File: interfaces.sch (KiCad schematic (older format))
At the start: 55 parts, among them J6 0878311420, J7 61300611121, U14 XC7A100T-FGG484, U17 EMMC04G-S100-B08U, U18 MAX3421EEHJ, U19 FT245RQ, U6 NVT2008DQ,115, Y1 ABM8G-12.000MHZ-18-D2Y-T

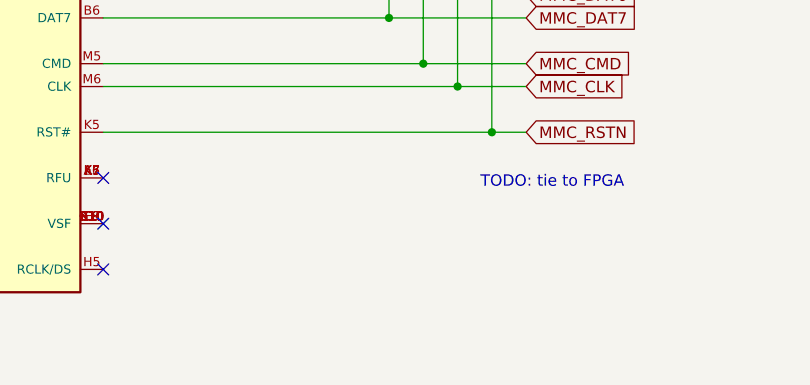
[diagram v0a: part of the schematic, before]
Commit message: Specify eMMC model
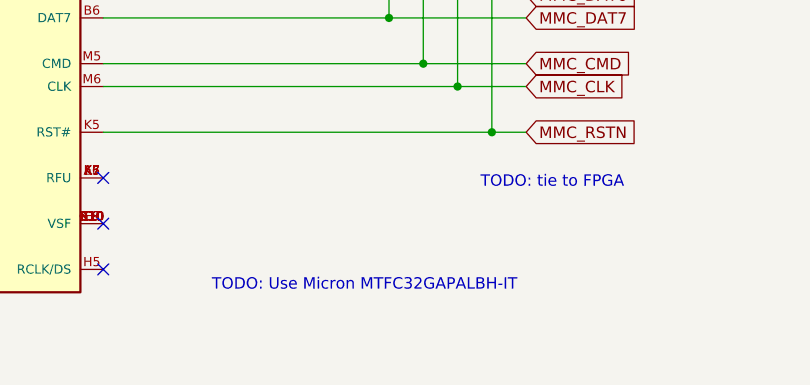
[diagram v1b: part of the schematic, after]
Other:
- note added: "TODO: Use Micron MTFC32GAPALBH-IT"
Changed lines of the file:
@@
 Text GLabel 8725 6150 0    50   Input ~ 0
 SPI0_CLK
+Text Notes 5125 10800 0    50   ~ 0
+TODO: Use Micron MTFC32GAPALBH-IT
 $EndSCHEMATC

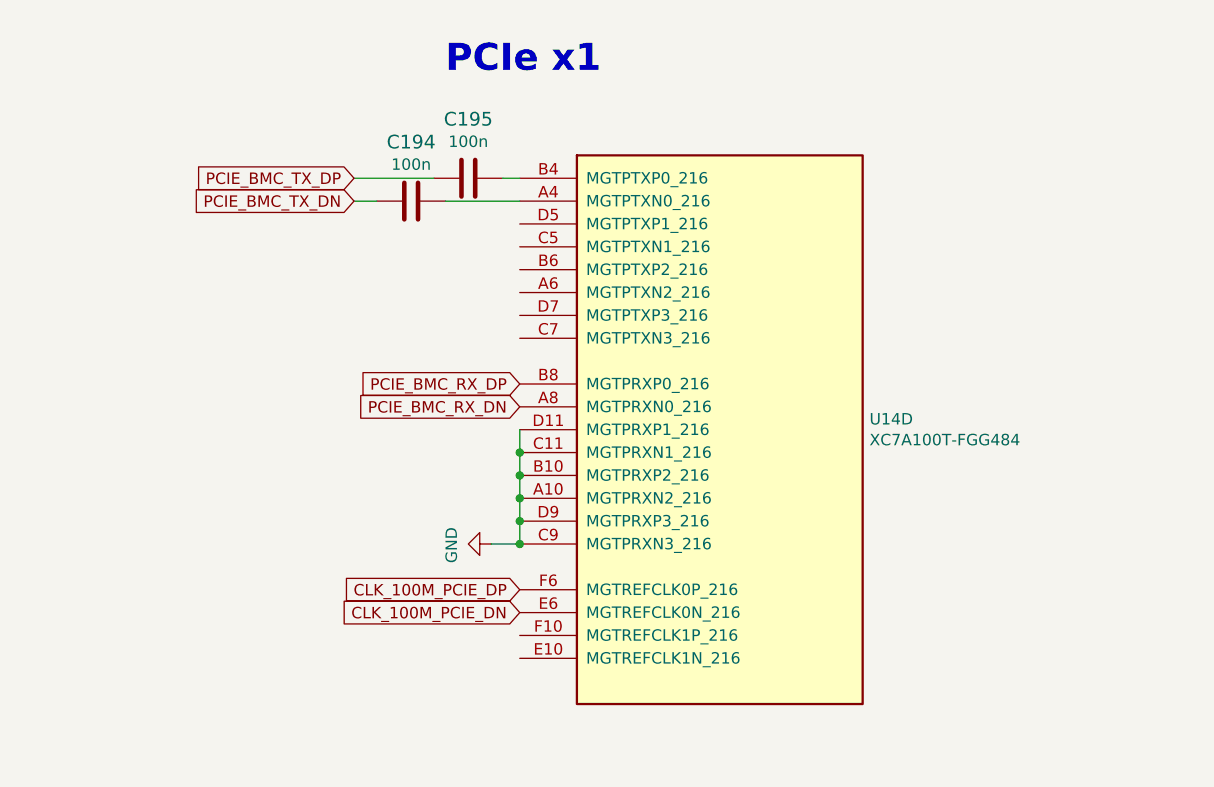
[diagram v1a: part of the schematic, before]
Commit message: Add BMC PCIe net classes
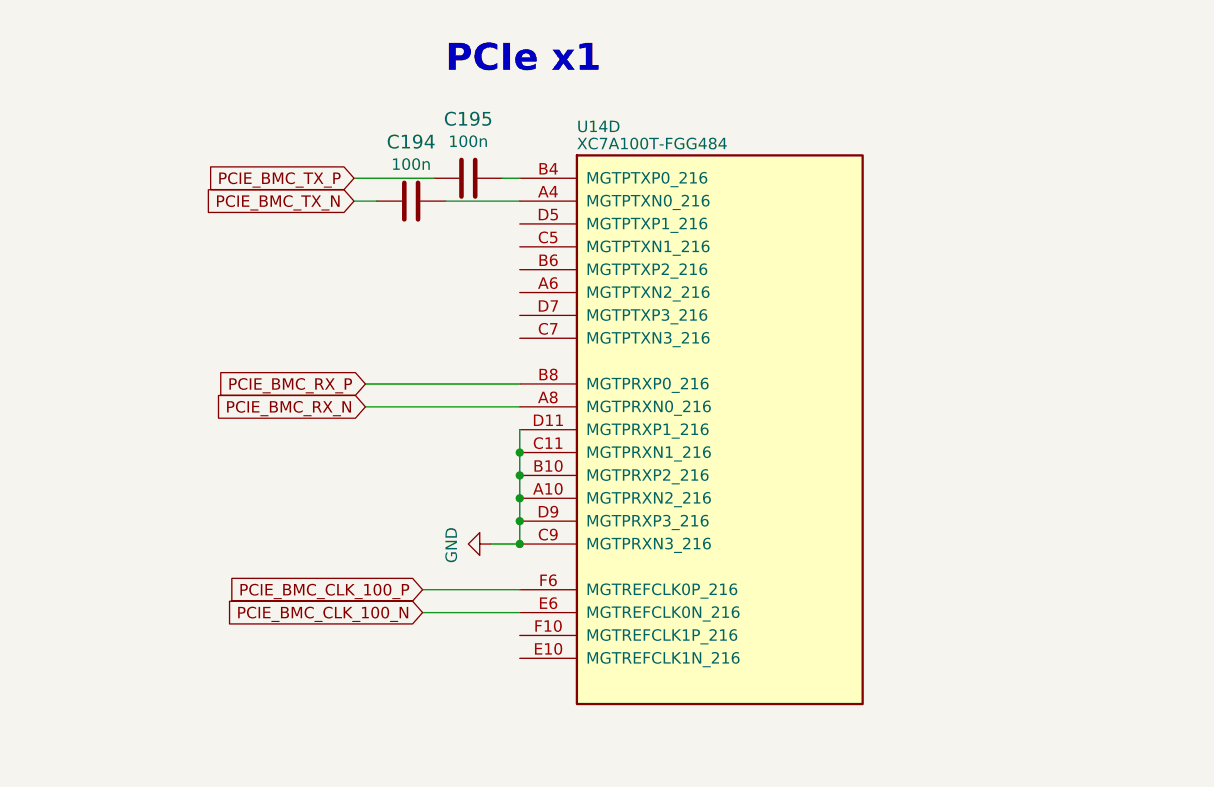
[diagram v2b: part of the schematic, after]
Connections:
- net CLK_100M_PCIE_DN renamed PCIE_BMC_CLK_100_N
- net CLK_100M_PCIE_DP renamed PCIE_BMC_CLK_100_P
- net PCIE_BMC_RX_DN renamed PCIE_BMC_RX_N
- net PCIE_BMC_RX_DP renamed PCIE_BMC_RX_P
- net PCIE_BMC_TX_DN renamed PCIE_BMC_TX_N
- net PCIE_BMC_TX_DP renamed PCIE_BMC_TX_P
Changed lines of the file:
@@
 U 4 1 603098D4
 P 7475 2850
-F 0 "U14" H 7505 2896 50  0000 L CNN
-F 1 "XC7A100T-FGG484" H 7505 2805 50  0000 L CNN
+F 0 "U14" H 6225 4175 50  0000 L CNN
+F 1 "XC7A100T-FGG484" H 6225 4100 50  0000 L CNN
 F 2 "artix-dc-scm-footprints:Xilinx_FGG484" H 7175 2850 50  0001 C CNN
 F 3 "" H 7175 2850 50  0000 C CNN
@@
 	1    0    0    -1
 $EndComp
-Text GLabel 5975 3550 0    50   Input ~ 0
-CLK_100M_PCIE_DP
-Text GLabel 5975 3650 0    50   Input ~ 0
-CLK_100M_PCIE_DN
-Text GLabel 5250 1750 0    50   Input ~ 0
-PCIE_BMC_TX_DP
-Text GLabel 5250 1850 0    50   Input ~ 0
-PCIE_BMC_TX_DN
-Text GLabel 5975 2650 0    50   Input ~ 0
-PCIE_BMC_RX_DP
-Text GLabel 5975 2750 0    50   Input ~ 0
-PCIE_BMC_RX_DN
 $Comp
 L artix-dc-scm:C_100n_0402-artix-dc-scm C195
@@
 Text Notes 5125 10800 0    50   ~ 0
 TODO: Use Micron MTFC32GAPALBH-IT
+Text GLabel 5550 3550 0    50   Input ~ 0
+PCIE_BMC_CLK_100_P
+Text GLabel 5550 3650 0    50   Input ~ 0
+PCIE_BMC_CLK_100_N
+Text GLabel 5250 1750 0    50   Input ~ 0
+PCIE_BMC_TX_P
+Text GLabel 5250 1850 0    50   Input ~ 0
+PCIE_BMC_TX_N
+Text GLabel 5300 2650 0    50   Input ~ 0
+PCIE_BMC_RX_P
+Text GLabel 5300 2750 0    50   Input ~ 0
+PCIE_BMC_RX_N
+Wire Wire Line
+	5975 3550 5550 3550
+Wire Wire Line
+	5975 3650 5550 3650
+Wire Wire Line
+	5300 2650 5975 2650
+Wire Wire Line
+	5300 2750 5975 2750
 $EndSCHEMATC

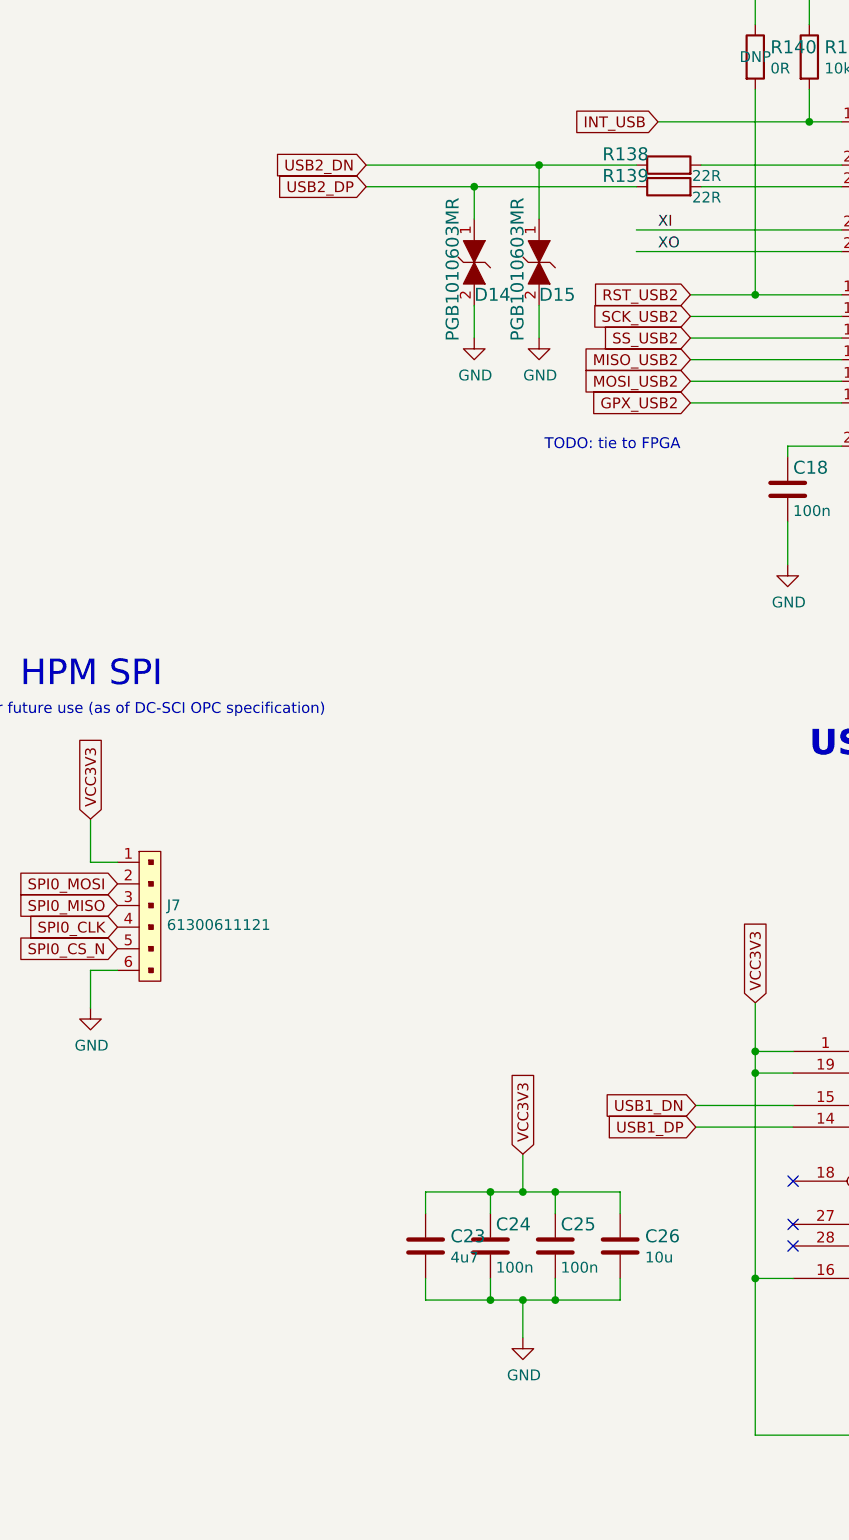
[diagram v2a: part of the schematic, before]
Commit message: Define USB diff lanes
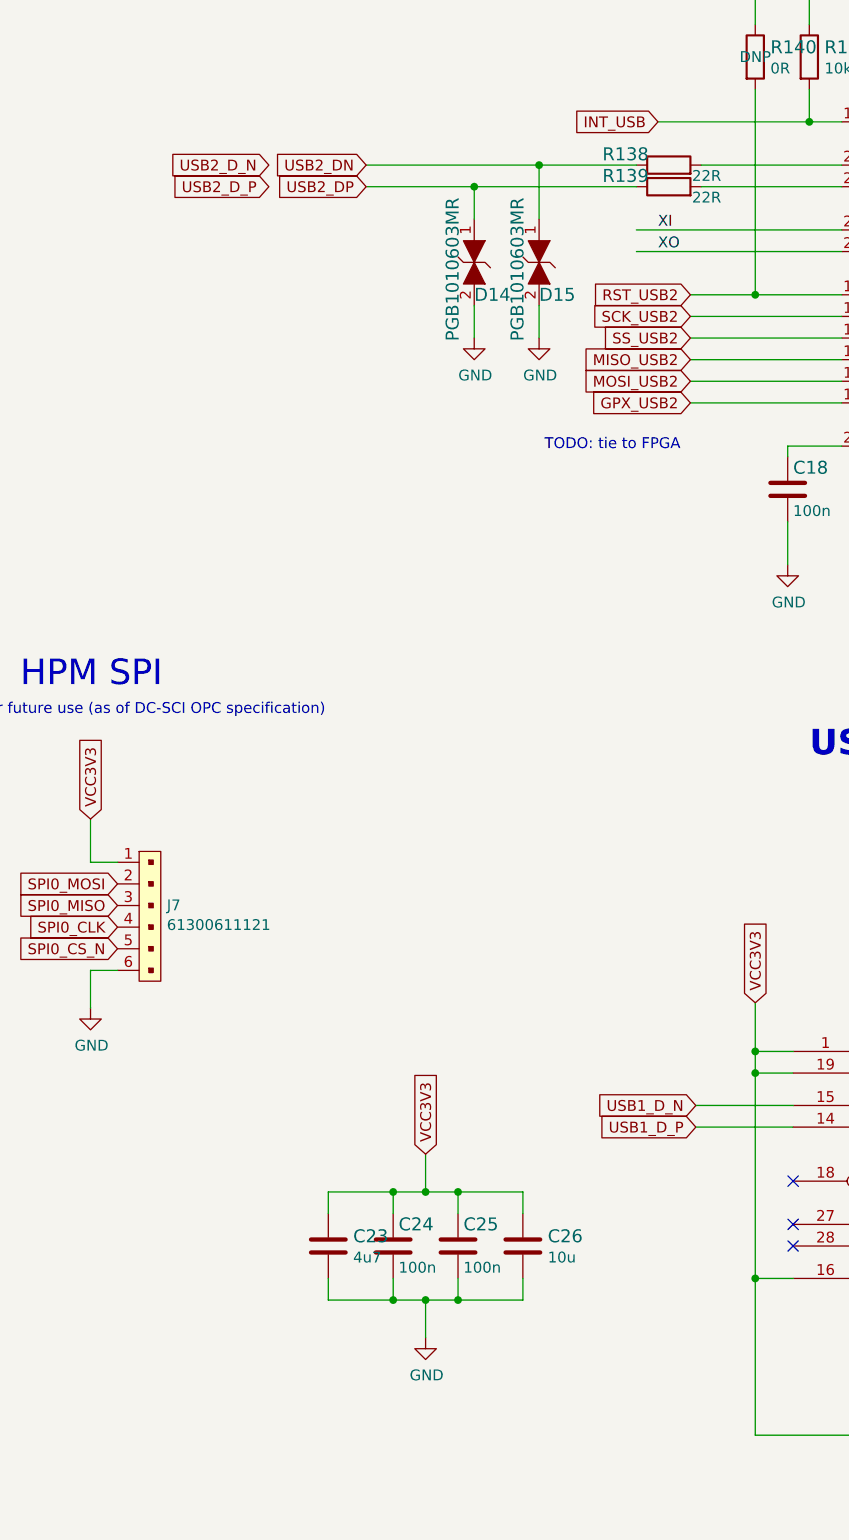
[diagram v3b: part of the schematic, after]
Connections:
- net USB1_DN renamed USB1_D_N
- net USB1_DP renamed USB1_D_P
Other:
- moved on the sheet: C23, C24, C25, C26
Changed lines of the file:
@@
 Wire Wire Line
 	11850 7075 11400 7075
-Text GLabel 11400 6975 0    50   Input ~ 0
-USB1_DN
-Text GLabel 11400 7075 0    50   Input ~ 0
-USB1_DP
 NoConn ~ 11850 7325
 NoConn ~ 11850 7525
@@
 L artix-dc-scm:C_100n_0402-artix-dc-scm C25
 U 1 1 625E9A3D
-P 10750 7625
-F 0 "C25" H 10775 7725 60  0000 L CNN
-F 1 "C_100n_0402" H 10750 7475 60  0001 C CNN
-F 2 "artix-dc-scm-footprints:0402-cap" H 10950 7825 60  0001 L CNN
-F 3 "" H 10750 7625 50  0001 C CNN
-F 4 "Walsin" H 10950 8025 60  0001 L CNN "Manufacturer"
-F 5 "0402X104K6R3CT" H 10950 7925 60  0001 L CNN "MPN"
-F 6 "100n" H 10775 7525 50  0000 L CNN "Val"
-	1    10750 7625
+P 10300 7625
+F 0 "C25" H 10325 7725 60  0000 L CNN
+F 1 "C_100n_0402" H 10300 7475 60  0001 C CNN
+F 2 "artix-dc-scm-footprints:0402-cap" H 10500 7825 60  0001 L CNN
+F 3 "" H 10300 7625 50  0001 C CNN
+F 4 "Walsin" H 10500 8025 60  0001 L CNN "Manufacturer"
+F 5 "0402X104K6R3CT" H 10500 7925 60  0001 L CNN "MPN"
+F 6 "100n" H 10325 7525 50  0000 L CNN "Val"
+	1    10300 7625
 	1    0    0    -1
 $EndComp
@@
 L artix-dc-scm:C_10u_0402 C26
 U 1 1 627E1224
-P 11050 7625
-F 0 "C26" H 11165 7670 60  0000 L CNN
-F 1 "C_10u_0402" H 11050 7475 60  0001 C CNN
-F 2 "artix-dc-scm-footprints:0402-cap" H 11250 7825 60  0001 L CNN
-F 3 "" H 11050 7625 50  0001 C CNN
-F 4 "MURATA" H 11250 8025 60  0001 L CNN "Manufacturer"
-F 5 "GRM155R60J106ME44D" H 11250 7925 60  0001 L CNN "MPN"
-F 6 "10u" H 11165 7572 50  0000 L CNN "Val"
-	1    11050 7625
+P 10600 7625
+F 0 "C26" H 10715 7670 60  0000 L CNN
+F 1 "C_10u_0402" H 10600 7475 60  0001 C CNN
+F 2 "artix-dc-scm-footprints:0402-cap" H 10800 7825 60  0001 L CNN
+F 3 "" H 10600 7625 50  0001 C CNN
+F 4 "MURATA" H 10800 8025 60  0001 L CNN "Manufacturer"
+F 5 "GRM155R60J106ME44D" H 10800 7925 60  0001 L CNN "MPN"
+F 6 "10u" H 10715 7572 50  0000 L CNN "Val"
+	1    10600 7625
 	1    0    0    -1
 $EndComp
@@
 L artix-dc-scm:C_100n_0402-artix-dc-scm C24
 U 1 1 62805326
-P 10450 7625
-F 0 "C24" H 10475 7725 60  0000 L CNN
-F 1 "C_100n_0402" H 10450 7475 60  0001 C CNN
-F 2 "artix-dc-scm-footprints:0402-cap" H 10650 7825 60  0001 L CNN
-F 3 "" H 10450 7625 50  0001 C CNN
-F 4 "Walsin" H 10650 8025 60  0001 L CNN "Manufacturer"
-F 5 "0402X104K6R3CT" H 10650 7925 60  0001 L CNN "MPN"
-F 6 "100n" H 10475 7525 50  0000 L CNN "Val"
-	1    10450 7625
+P 10000 7625
+F 0 "C24" H 10025 7725 60  0000 L CNN
+F 1 "C_100n_0402" H 10000 7475 60  0001 C CNN
+F 2 "artix-dc-scm-footprints:0402-cap" H 10200 7825 60  0001 L CNN
+F 3 "" H 10000 7625 50  0001 C CNN
+F 4 "Walsin" H 10200 8025 60  0001 L CNN "Manufacturer"
+F 5 "0402X104K6R3CT" H 10200 7925 60  0001 L CNN "MPN"
+F 6 "100n" H 10025 7525 50  0000 L CNN "Val"
+	1    10000 7625
 	1    0    0    -1
 $EndComp
@@
 L artix-dc-scm:C_4u7_0402 C23
 U 1 1 628061B5
-P 10150 7625
-F 0 "C23" H 10265 7670 60  0000 L CNN
-F 1 "C_4u7_0402" H 10150 7475 60  0001 C CNN
-F 2 "artix-dc-scm-footprints:0402-cap" H 10350 7825 60  0001 L CNN
-F 3 "" H 10150 7625 50  0001 C CNN
-F 4 "MURATA" H 10350 8025 60  0001 L CNN "Manufacturer"
-F 5 "GRM155R61A475MEAAD" H 10350 7925 60  0001 L CNN "MPN"
-F 6 "4u7" H 10265 7572 50  0000 L CNN "Val"
-	1    10150 7625
+P 9700 7625
+F 0 "C23" H 9815 7670 60  0000 L CNN
+F 1 "C_4u7_0402" H 9700 7475 60  0001 C CNN
+F 2 "artix-dc-scm-footprints:0402-cap" H 9900 7825 60  0001 L CNN
+F 3 "" H 9700 7625 50  0001 C CNN
+F 4 "MURATA" H 9900 8025 60  0001 L CNN "Manufacturer"
+F 5 "GRM155R61A475MEAAD" H 9900 7925 60  0001 L CNN "MPN"
+F 6 "4u7" H 9815 7572 50  0000 L CNN "Val"
+	1    9700 7625
 	1    0    0    -1
 $EndComp
@@
 Connection ~ 11675 7775
 Wire Wire Line
-	11050 7475 11050 7375
-Wire Wire Line
-	11050 7375 10750 7375
-Wire Wire Line
-	10150 7375 10150 7475
-Wire Wire Line
-	10450 7475 10450 7375
-Connection ~ 10450 7375
-Wire Wire Line
-	10450 7375 10150 7375
-Wire Wire Line
-	10750 7475 10750 7375
-Connection ~ 10750 7375
-Wire Wire Line
-	10750 7375 10600 7375
-Wire Wire Line
-	10150 7775 10150 7875
-Wire Wire Line
-	10150 7875 10450 7875
-Wire Wire Line
-	11050 7875 11050 7775
-Wire Wire Line
-	10750 7775 10750 7875
-Connection ~ 10750 7875
-Wire Wire Line
-	10750 7875 11050 7875
-Wire Wire Line
-	10450 7775 10450 7875
-Connection ~ 10450 7875
-Wire Wire Line
-	10450 7875 10600 7875
-Wire Wire Line
-	10600 7875 10600 8050
-Connection ~ 10600 7875
-Wire Wire Line
-	10600 7875 10750 7875
+	10600 7475 10600 7375
+Wire Wire Line
+	10600 7375 10300 7375
+Wire Wire Line
+	9700 7375 9700 7475
+Wire Wire Line
+	10000 7475 10000 7375
+Connection ~ 10000 7375
+Wire Wire Line
+	10000 7375 9700 7375
+Wire Wire Line
+	10300 7475 10300 7375
+Connection ~ 10300 7375
+Wire Wire Line
+	10300 7375 10150 7375
+Wire Wire Line
+	9700 7775 9700 7875
+Wire Wire Line
+	9700 7875 10000 7875
+Wire Wire Line
+	10600 7875 10600 7775
+Wire Wire Line
+	10300 7775 10300 7875
+Connection ~ 10300 7875
+Wire Wire Line
+	10300 7875 10600 7875
+Wire Wire Line
+	10000 7775 10000 7875
+Connection ~ 10000 7875
+Wire Wire Line
+	10000 7875 10150 7875
+Wire Wire Line
+	10150 7875 10150 8050
+Connection ~ 10150 7875
+Wire Wire Line
+	10150 7875 10300 7875
 $Comp
 L artix-dc-scm:GND-artix-dc-scm #PWR090
 U 1 1 628F287E
-P 10600 8050
-F 0 "#PWR090" H 10600 7800 50  0001 C CNN
-F 1 "GND" H 10605 7877 50  0000 C CNN
-F 2 "" H 10600 8050 50  0001 C CNN
-F 3 "" H 10600 8050 50  0001 C CNN
-	1    10600 8050
-	1    0    0    -1
-$EndComp
-Wire Wire Line
-	10600 7375 10600 7200
-Connection ~ 10600 7375
-Wire Wire Line
-	10600 7375 10450 7375
-Text GLabel 10600 7200 1    50   Input ~ 0
+P 10150 8050
+F 0 "#PWR090" H 10150 7800 50  0001 C CNN
+F 1 "GND" H 10155 7877 50  0000 C CNN
+F 2 "" H 10150 8050 50  0001 C CNN
+F 3 "" H 10150 8050 50  0001 C CNN
+	1    10150 8050
+	1    0    0    -1
+$EndComp
+Wire Wire Line
+	10150 7375 10150 7200
+Connection ~ 10150 7375
+Wire Wire Line
+	10150 7375 10000 7375
+Text GLabel 10150 7200 1    50   Input ~ 0
 VCC3V3
 Text Notes 14425 7250 0    50   ~ 0
@@
 Wire Wire Line
 	5300 2750 5975 2750
+Text GLabel 9425 2725 0    50   Input ~ 0
+USB2_D_P
+Text GLabel 9425 2625 0    50   Input ~ 0
+USB2_D_N
+Text GLabel 11400 7075 0    50   Input ~ 0
+USB1_D_P
+Text GLabel 11400 6975 0    50   Input ~ 0
+USB1_D_N
 $EndSCHEMATC

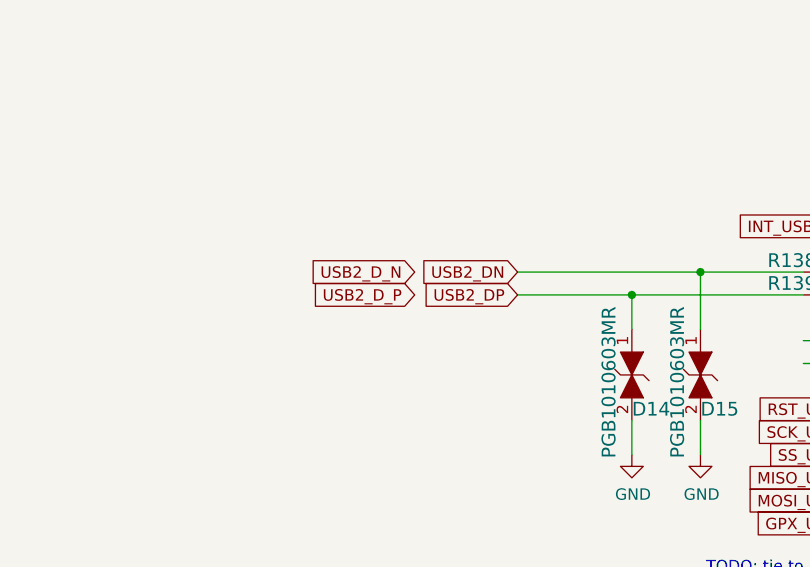
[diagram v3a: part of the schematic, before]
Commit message: Route low speed HPM control signals
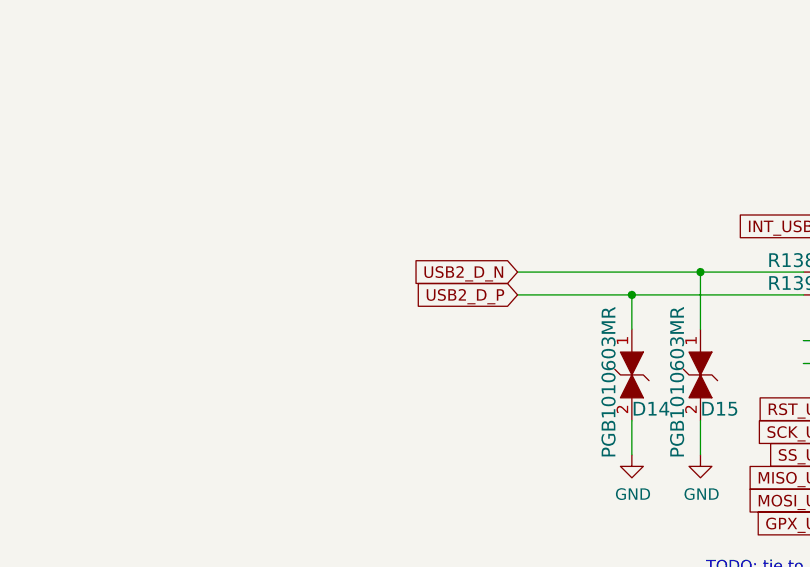
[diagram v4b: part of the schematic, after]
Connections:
- net USB2_DN is gone; now on net USB2_D_N: D15.1, R138.1
- net USB2_DP is gone; now on net USB2_D_P: D14.1, R139.1
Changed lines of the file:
@@
 	0    1    1    0
 $EndComp
-Text GLabel 9875 2625 0    50   Input ~ 0
-USB2_DN
-Text GLabel 9875 2725 0    50   Input ~ 0
-USB2_DP
 Text GLabel 11375 3225 0    50   Input ~ 0
 RST_USB2
@@
 Wire Wire Line
 	5300 2750 5975 2750
-Text GLabel 9425 2725 0    50   Input ~ 0
+Text GLabel 9875 2725 0    50   Input ~ 0
 USB2_D_P
-Text GLabel 9425 2625 0    50   Input ~ 0
+Text GLabel 9875 2625 0    50   Input ~ 0
 USB2_D_N
 Text GLabel 11400 7075 0    50   Input ~ 0
